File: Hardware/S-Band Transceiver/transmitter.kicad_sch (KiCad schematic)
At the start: 40 parts, among them J5 SMA, U10 TSS-53LNB3+, U11 DCW-22-332+, U12 ADL5906, U7 DAT-31A+, U8 PE44820, U9 SN74LVC1G125DCK

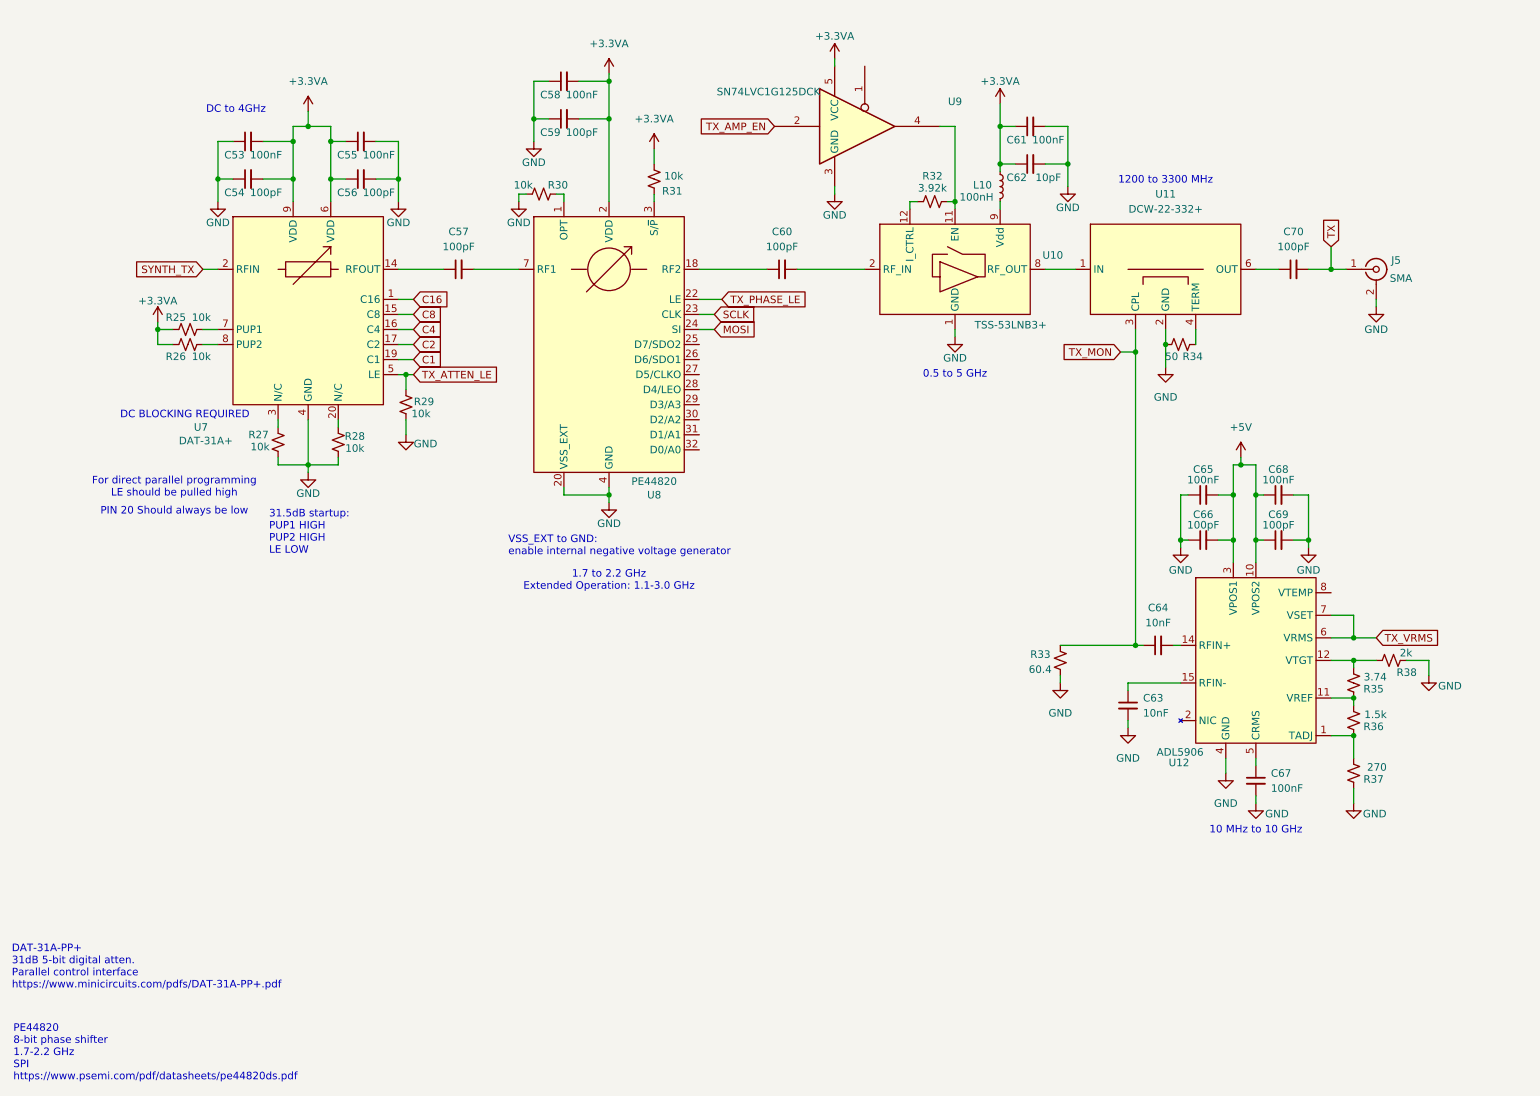
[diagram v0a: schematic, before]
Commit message: Updating Capacitors and LEDs in schematic
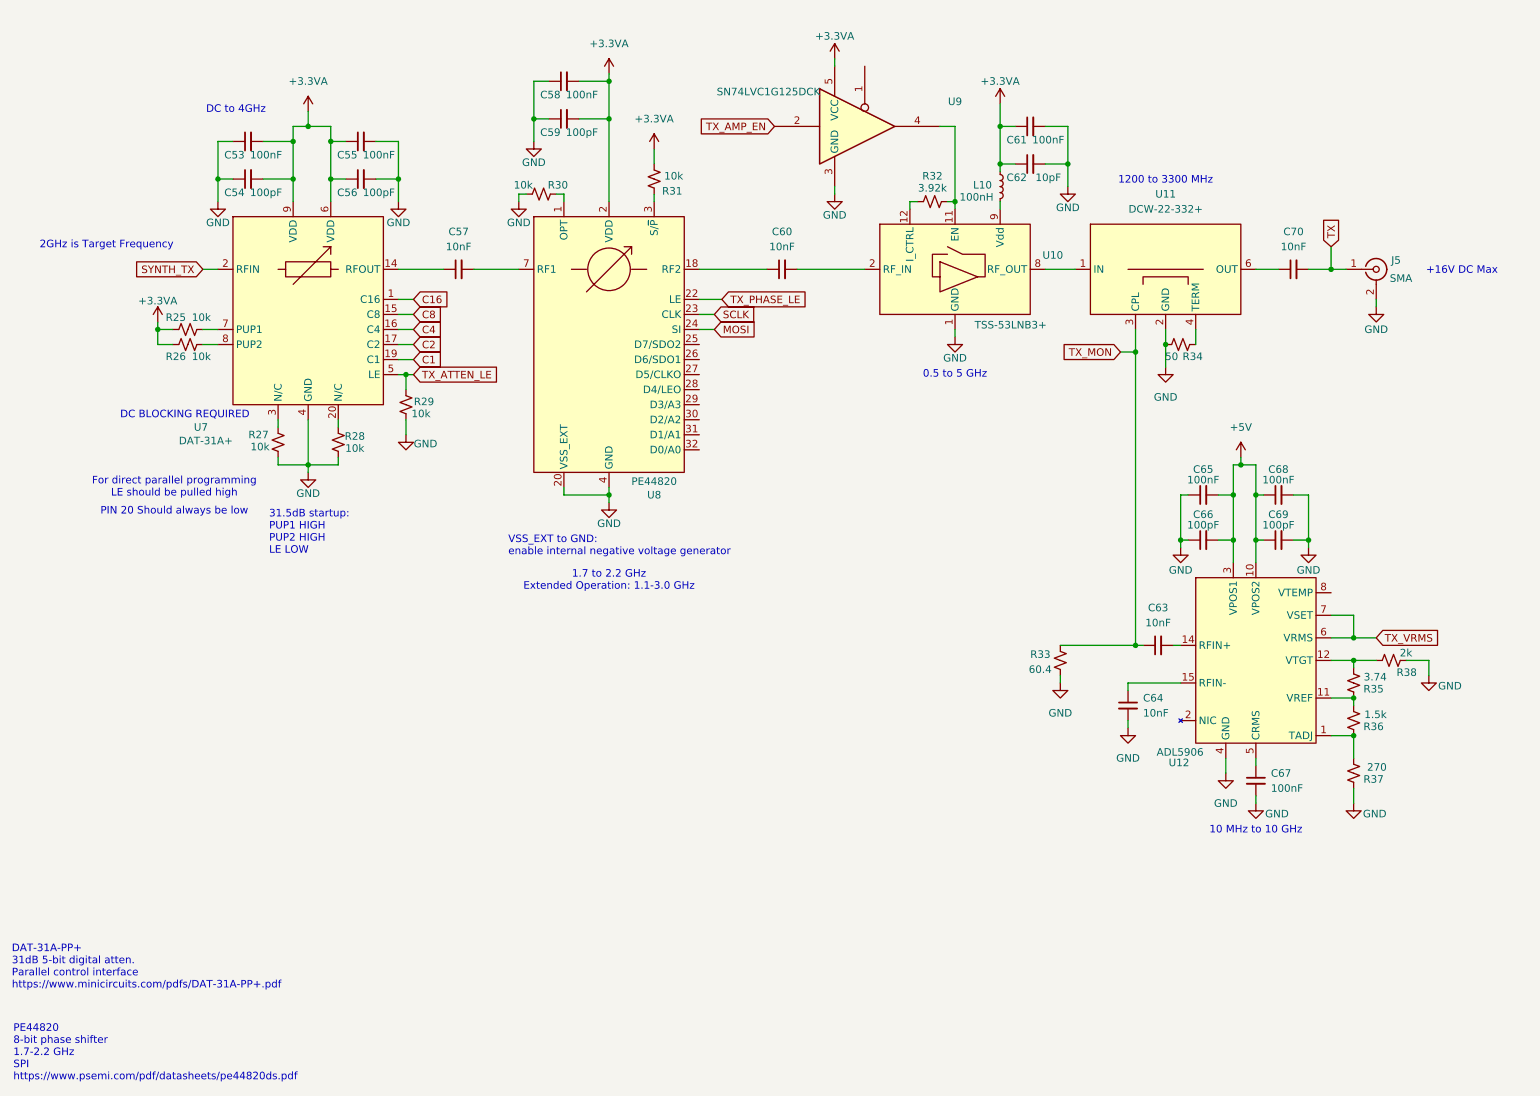
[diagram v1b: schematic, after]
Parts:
- C57, C60, C70: value 100pF -> 10nF; Digikey (none) -> 1284-1540-1-ND
- C63, C64: Digikey (none) -> 1284-1540-1-ND
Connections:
- net GND: now also C64.2; no longer C63.2
- net TX_MON: now also C63.1; no longer C64.1
- net at U12.14 (RFIN+): now also C63.2; no longer C64.2
- net at U12.15 (RFIN-): now also C64.1; no longer C63.1
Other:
- note added: "+16V DC Max"
- note added: "2GHz is Target Frequency"
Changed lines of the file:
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@@
 		)
 	)
+	(text "+16V DC Max"
+		(exclude_from_sim no)
+		(at 262.128 56.134 0)
+		(effects
+			(font
+				(size 1.27 1.27)
+			)
+		)
+	)
 	(text "DC to 4GHz"
 		(exclude_from_sim no)
@@
 		)
 	)
+	(text "2GHz is Target Frequency"
+		(exclude_from_sim no)
+		(at 33.274 51.816 0)
+		(effects
+			(font
+				(size 1.27 1.27)
+			)
+		)
+	)
 	(text "VSS_EXT to GND:\nenable internal negative voltage generator\n"
 		(exclude_from_sim no)
@@
 	)
 	(symbol
-		(lib_id "Device:C_Small")
-		(at 147.32 55.88 90)
-		(unit 1)
-		(exclude_from_sim no)
-		(in_bom yes)
-		(on_board yes)
-		(dnp no)
-		(fields_autoplaced yes)
-		(property "Reference" "C60"
-			(at 147.3263 49.53 90)
-			(effects
-				(font
-					(size 1.27 1.27)
-				)
-			)
-		)
-		(property "Value" "100pF"
-			(at 147.3263 52.07 90)
-			(effects
-				(font
-					(size 1.27 1.27)
-				)
-			)
-		)
-		(property "Footprint" "Capacitor_SMD:C_0402_1005Metric"
-			(at 147.32 55.88 0)
-			(effects
-				(font
-					(size 1.27 1.27)
-				)
-				(hide yes)
-			)
-		)
-		(property "Datasheet" "~"
-			(at 147.32 55.88 0)
-			(effects
-				(font
-					(size 1.27 1.27)
-				)
-				(hide yes)
-			)
-		)
-		(property "Description" "Unpolarized capacitor, small symbol"
-			(at 147.32 55.88 0)
-			(effects
-				(font
-					(size 1.27 1.27)
-				)
-				(hide yes)
-			)
-		)
-		(pin "1"
-		)
-		(pin "2"
-		)
-		(instances
-			(project "S-Band Transceiver"
-				(path "/811f57cf-e3df-4fba-aff9-353adc85299e/bd41cfbd-cb46-4539-92e1-7ba2287bca8a"
-					(reference "C60")
-					(unit 1)
-				)
-			)
-		)
-	)
-	(symbol
 		(lib_id "_tim-RF:ADL5906")
 		(at 227.33 121.92 0)
@@
 		(dnp no)
 		(fields_autoplaced yes)
-		(property "Reference" "C64"
+		(property "Reference" "C63"
 			(at 210.8263 113.03 90)
 			(effects
@@
 			)
 		)
-		(property "Datasheet" "~"
+		(property "Datasheet" "https://www.mouser.com/datasheet/2/40/520l-1902329.pdf"
 			(at 210.82 119.38 0)
 			(effects
@@
 			)
 		)
-		(pin "2"
+		(property "Digikey" "1284-1540-1-ND"
+			(at 210.82 119.38 90)
+			(effects
+				(font
+					(size 1.27 1.27)
+				)
+				(hide yes)
+			)
 		)
 		(pin "1"
 		)
+		(pin "2"
+		)
 		(instances
 			(project "S-Band Transceiver"
 				(path "/811f57cf-e3df-4fba-aff9-353adc85299e/bd41cfbd-cb46-4539-92e1-7ba2287bca8a"
-					(reference "C64")
+					(reference "C63")
 					(unit 1)
 				)
@@
 	(symbol
 		(lib_id "Device:C_Small")
-		(at 205.74 129.54 0)
+		(at 147.32 55.88 90)
 		(unit 1)
 		(exclude_from_sim no)
@@
 		(dnp no)
 		(fields_autoplaced yes)
-		(property "Reference" "C63"
-			(at 208.28 128.2762 0)
+		(property "Reference" "C60"
+			(at 147.3263 49.53 90)
 			(effects
 				(font
 					(size 1.27 1.27)
 				)
-				(justify left)
 			)
 		)
 		(property "Value" "10nF"
-			(at 208.28 130.8162 0)
+			(at 147.3263 52.07 90)
 			(effects
 				(font
 					(size 1.27 1.27)
 				)
-				(justify left)
 			)
 		)
 		(property "Footprint" "Capacitor_SMD:C_0402_1005Metric"
-			(at 205.74 129.54 0)
+			(at 147.32 55.88 0)
 			(effects
 				(font
@@
 			)
 		)
-		(property "Datasheet" "~"
-			(at 205.74 129.54 0)
+		(property "Datasheet" "https://www.mouser.com/datasheet/2/40/520l-1902329.pdf"
+			(at 147.32 55.88 0)
 			(effects
 				(font
@@
 		)
 		(property "Description" "Unpolarized capacitor, small symbol"
-			(at 205.74 129.54 0)
+			(at 147.32 55.88 0)
 			(effects
 				(font
@@
 			)
 		)
-		(pin "2"
+		(property "Digikey" "1284-1540-1-ND"
+			(at 147.32 55.88 90)
+			(effects
+				(font
+					(size 1.27 1.27)
+				)
+				(hide yes)
+			)
 		)
 		(pin "1"
 		)
+		(pin "2"
+		)
 		(instances
 			(project "S-Band Transceiver"
 				(path "/811f57cf-e3df-4fba-aff9-353adc85299e/bd41cfbd-cb46-4539-92e1-7ba2287bca8a"
-					(reference "C63")
+					(reference "C60")
 					(unit 1)
 				)
@@
 	)
 	(symbol
+		(lib_id "Device:C_Small")
+		(at 205.74 129.54 0)
+		(unit 1)
+		(exclude_from_sim no)
+		(in_bom yes)
+		(on_board yes)
+		(dnp no)
+		(fields_autoplaced yes)
+		(property "Reference" "C64"
+			(at 208.28 128.2762 0)
+			(effects
+				(font
+					(size 1.27 1.27)
+				)
+				(justify left)
+			)
+		)
+		(property "Value" "10nF"
+			(at 208.28 130.8162 0)
+			(effects
+				(font
+					(size 1.27 1.27)
+				)
+				(justify left)
+			)
+		)
+		(property "Footprint" "Capacitor_SMD:C_0402_1005Metric"
+			(at 205.74 129.54 0)
+			(effects
+				(font
+					(size 1.27 1.27)
+				)
+				(hide yes)
+			)
+		)
+		(property "Datasheet" "https://www.mouser.com/datasheet/2/40/520l-1902329.pdf"
+			(at 205.74 129.54 0)
+			(effects
+				(font
+					(size 1.27 1.27)
+				)
+				(hide yes)
+			)
+		)
+		(property "Description" "Unpolarized capacitor, small symbol"
+			(at 205.74 129.54 0)
+			(effects
+				(font
+					(size 1.27 1.27)
+				)
+				(hide yes)
+			)
+		)
+		(property "Digikey" "1284-1540-1-ND"
+			(at 205.74 129.54 90)
+			(effects
+				(font
+					(size 1.27 1.27)
+				)
+				(hide yes)
+			)
+		)
+		(pin "1"
+		)
+		(pin "2"
+		)
+		(instances
+			(project "S-Band Transceiver"
+				(path "/811f57cf-e3df-4fba-aff9-353adc85299e/bd41cfbd-cb46-4539-92e1-7ba2287bca8a"
+					(reference "C64")
+					(unit 1)
+				)
+			)
+		)
+	)
+	(symbol
 		(lib_id "power:GND")
 		(at 212.09 72.39 0)
@@
 	)
 	(symbol
-		(lib_id "Device:C_Small")
-		(at 92.71 55.88 90)
-		(unit 1)
-		(exclude_from_sim no)
-		(in_bom yes)
-		(on_board yes)
-		(dnp no)
-		(fields_autoplaced yes)
-		(property "Reference" "C57"
-			(at 92.7163 49.53 90)
-			(effects
-				(font
-					(size 1.27 1.27)
-				)
-			)
-		)
-		(property "Value" "100pF"
-			(at 92.7163 52.07 90)
-			(effects
-				(font
-					(size 1.27 1.27)
-				)
-			)
-		)
-		(property "Footprint" "Capacitor_SMD:C_0402_1005Metric"
-			(at 92.71 55.88 0)
-			(effects
-				(font
-					(size 1.27 1.27)
-				)
-				(hide yes)
-			)
-		)
-		(property "Datasheet" "~"
-			(at 92.71 55.88 0)
-			(effects
-				(font
-					(size 1.27 1.27)
-				)
-				(hide yes)
-			)
-		)
-		(property "Description" "Unpolarized capacitor, small symbol"
-			(at 92.71 55.88 0)
-			(effects
-				(font
-					(size 1.27 1.27)
-				)
-				(hide yes)
-			)
-		)
-		(pin "1"
-		)
-		(pin "2"
-		)
-		(instances
-			(project "S-Band Transceiver"
-				(path "/811f57cf-e3df-4fba-aff9-353adc85299e/bd41cfbd-cb46-4539-92e1-7ba2287bca8a"
-					(reference "C57")
-					(unit 1)
-				)
-			)
-		)
-	)
-	(symbol
 		(lib_id "power:GND")
 		(at 227.33 146.05 0)
@@
 			)
 		)
-		(property "Value" "100pF"
+		(property "Value" "10nF"
 			(at 233.6863 52.07 90)
 			(effects
@@
 			)
 		)
-		(property "Datasheet" "~"
+		(property "Datasheet" "https://www.mouser.com/datasheet/2/40/520l-1902329.pdf"
 			(at 233.68 55.88 0)
 			(effects
@@
 			)
 		)
+		(property "Digikey" "1284-1540-1-ND"
+			(at 233.68 55.88 90)
+			(effects
+				(font
+					(size 1.27 1.27)
+				)
+				(hide yes)
+			)
+		)
 		(pin "1"
 		)
@@
 					(unit 1)
 				)
+			)
+		)
+	)
+	(symbol
+		(lib_id "Device:C_Small")
+		(at 92.71 55.88 90)
+		(unit 1)
+		(exclude_from_sim no)
+		(in_bom yes)
+		(on_board yes)
+		(dnp no)
+		(fields_autoplaced yes)
+		(property "Reference" "C57"
+			(at 92.7163 49.53 90)
+			(effects
+				(font
+					(size 1.27 1.27)
+				)
+			)
+		)
+		(property "Value" "10nF"
+			(at 92.7163 52.07 90)
+			(effects
+				(font
+					(size 1.27 1.27)
+				)
+			)
+		)
+		(property "Footprint" "Capacitor_SMD:C_0402_1005Metric"
+			(at 92.71 55.88 0)
+			(effects
+				(font
+					(size 1.27 1.27)
+				)
+				(hide yes)
+			)
+		)
+		(property "Datasheet" "https://www.mouser.com/datasheet/2/40/520l-1902329.pdf"
+			(at 92.71 55.88 0)
+			(effects
+				(font
+					(size 1.27 1.27)
+				)
+				(hide yes)
+			)
+		)
+		(property "Description" "Unpolarized capacitor, small symbol"
+			(at 92.71 55.88 0)
+			(effects
+				(font
+					(size 1.27 1.27)
+				)
+				(hide yes)
+			)
+		)
+		(property "Digikey" "1284-1540-1-ND"
+			(at 92.71 55.88 90)
+			(effects
+				(font
+					(size 1.27 1.27)
+				)
+				(hide yes)
+			)
+		)
+		(pin "1"
+		)
+		(pin "2"
+		)
+		(instances
+			(project "S-Band Transceiver"
+				(path "/811f57cf-e3df-4fba-aff9-353adc85299e/bd41cfbd-cb46-4539-92e1-7ba2287bca8a"
+					(reference "C57")
+					(unit 1)
+				)

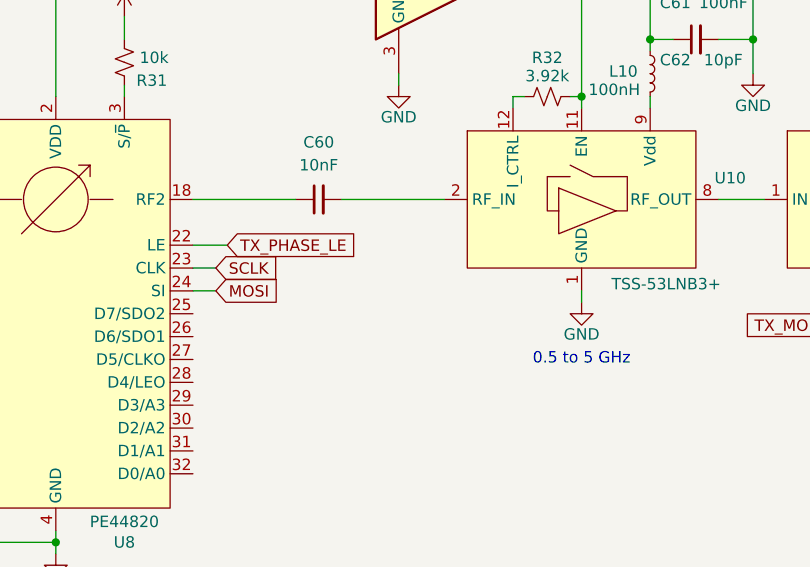
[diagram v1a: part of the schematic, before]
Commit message: Updating board layout, adding inductor to LNA input
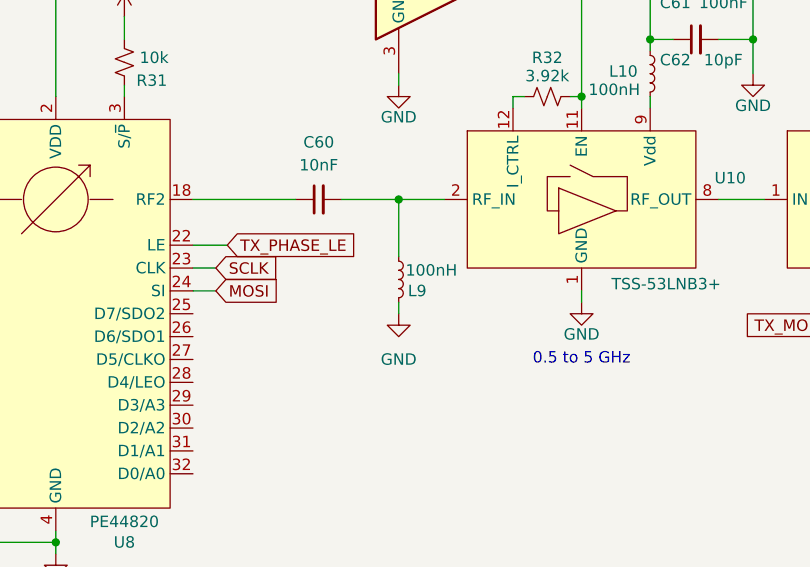
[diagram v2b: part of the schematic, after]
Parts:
- added L9: 100nH, Inductor_SMD:L_0402_1005Metric, symbol Device:L_Small
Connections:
- net GND: now also L9.2
- net at C60.2, U10.2 (RF_IN): now also L9.1
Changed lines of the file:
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@@
 	)
 	(junction
+		(at 156.21 55.88)
+		(diameter 0)
+		(color 0 0 0 0)
+	)
+	(junction
 		(at 207.01 119.38)
 		(diameter 0)
@@
 	(wire
 		(pts
+			(xy 156.21 67.31) (xy 156.21 68.58)
+		)
+		(stroke
+			(width 0)
+			(type default)
+		)
+	)
+	(wire
+		(pts
 			(xy 133.35 63.5) (xy 135.89 63.5)
 		)
@@
 	(wire
 		(pts
+			(xy 156.21 55.88) (xy 156.21 62.23)
+		)
+		(stroke
+			(width 0)
+			(type default)
+		)
+	)
+	(wire
+		(pts
 			(xy 105.41 24.13) (xy 105.41 30.48)
 		)
@@
 	(wire
 		(pts
+			(xy 156.21 55.88) (xy 161.29 55.88)
+		)
+		(stroke
+			(width 0)
+			(type default)
+		)
+	)
+	(wire
+		(pts
 			(xy 205.74 125.73) (xy 205.74 127)
 		)
@@
 	(wire
 		(pts
-			(xy 149.86 55.88) (xy 161.29 55.88)
+			(xy 149.86 55.88) (xy 156.21 55.88)
 		)
 		(stroke
@@
 	)
 	(symbol
+		(lib_id "Device:L_Small")
+		(at 156.21 64.77 0)
+		(unit 1)
+		(exclude_from_sim no)
+		(in_bom yes)
+		(on_board yes)
+		(dnp no)
+		(property "Reference" "L9"
+			(at 157.226 66.04 0)
+			(effects
+				(font
+					(size 1.27 1.27)
+				)
+				(justify left)
+			)
+		)
+		(property "Value" "100nH"
+			(at 156.972 63.754 0)
+			(effects
+				(font
+					(size 1.27 1.27)
+				)
+				(justify left)
+			)
+		)
+		(property "Footprint" "Inductor_SMD:L_0402_1005Metric"
+			(at 156.21 64.77 0)
+			(effects
+				(font
+					(size 1.27 1.27)
+				)
+				(hide yes)
+			)
+		)
+		(property "Datasheet" "~"
+			(at 156.21 64.77 0)
+			(effects
+				(font
+					(size 1.27 1.27)
+				)
+				(hide yes)
+			)
+		)
+		(property "Description" "Inductor, small symbol"
+			(at 156.21 64.77 0)
+			(effects
+				(font
+					(size 1.27 1.27)
+				)
+				(hide yes)
+			)
+		)
+		(pin "2"
+		)
+		(pin "1"
+		)
+		(instances
+			(project "S-Band Transceiver"
+				(path "/811f57cf-e3df-4fba-aff9-353adc85299e/bd41cfbd-cb46-4539-92e1-7ba2287bca8a"
+					(reference "L9")
+					(unit 1)
+				)
+			)
+		)
+	)
+	(symbol
 		(lib_id "Device:C_Small")
 		(at 57.15 34.29 90)
@@
 					(unit 1)
 				)
+			)
+		)
+	)
+	(symbol
+		(lib_id "power:GND")
+		(at 156.21 68.58 0)
+		(mirror y)
+		(unit 1)
+		(exclude_from_sim no)
+		(in_bom yes)
+		(on_board yes)
+		(dnp no)
+		(fields_autoplaced yes)
+		(property "Reference" "#PWR0137"
+			(at 156.21 74.93 0)
+			(effects
+				(font
+					(size 1.27 1.27)
+				)
+				(hide yes)
+			)
+		)
+		(property "Value" "GND"
+			(at 156.21 73.66 0)
+			(effects
+				(font
+					(size 1.27 1.27)
+				)
+			)
+		)
+		(property "Footprint" ""
+			(at 156.21 68.58 0)
+			(effects
+				(font
+					(size 1.27 1.27)
+				)
+				(hide yes)
+			)
+		)
+		(property "Datasheet" ""
+			(at 156.21 68.58 0)
+			(effects
+				(font
+					(size 1.27 1.27)
+				)
+				(hide yes)
+			)
+		)
+		(property "Description" "Power symbol creates a global label with name \"GND\" , ground"
+			(at 156.21 68.58 0)
+			(effects
+				(font
+					(size 1.27 1.27)
+				)
+				(hide yes)
+			)
+		)
+		(pin "1"
+		)
+		(instances
+			(project "S-Band Transceiver"
+				(path "/811f57cf-e3df-4fba-aff9-353adc85299e/bd41cfbd-cb46-4539-92e1-7ba2287bca8a"
+					(reference "#PWR0137")
+					(unit 1)
+				)

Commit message: Updating routing
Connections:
- net TX renamed TX OUT
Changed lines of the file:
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@@
 		)
 	)
-	(global_label "TX"
+	(global_label "TX OUT"
 		(shape input)
 		(at 240.03 52.07 90)
@@
 		)
 		(property "Intersheetrefs" "${INTERSHEET_REFS}"
-			(at 240.03 46.9077 90)
+			(at 240.03 42.3115 90)
 			(effects
 				(font
